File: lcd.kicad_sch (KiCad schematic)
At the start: 9 parts, among them J2 FPC-05F-12PH20, Q1 SS8050

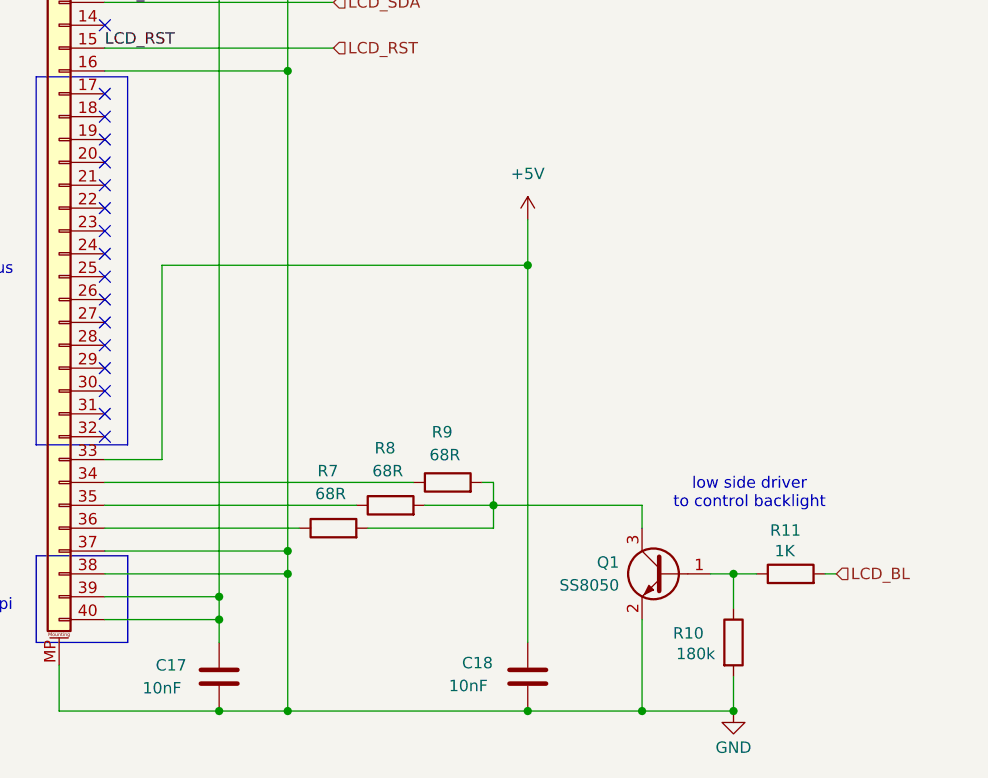
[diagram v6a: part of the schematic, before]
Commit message: small updates in component selection
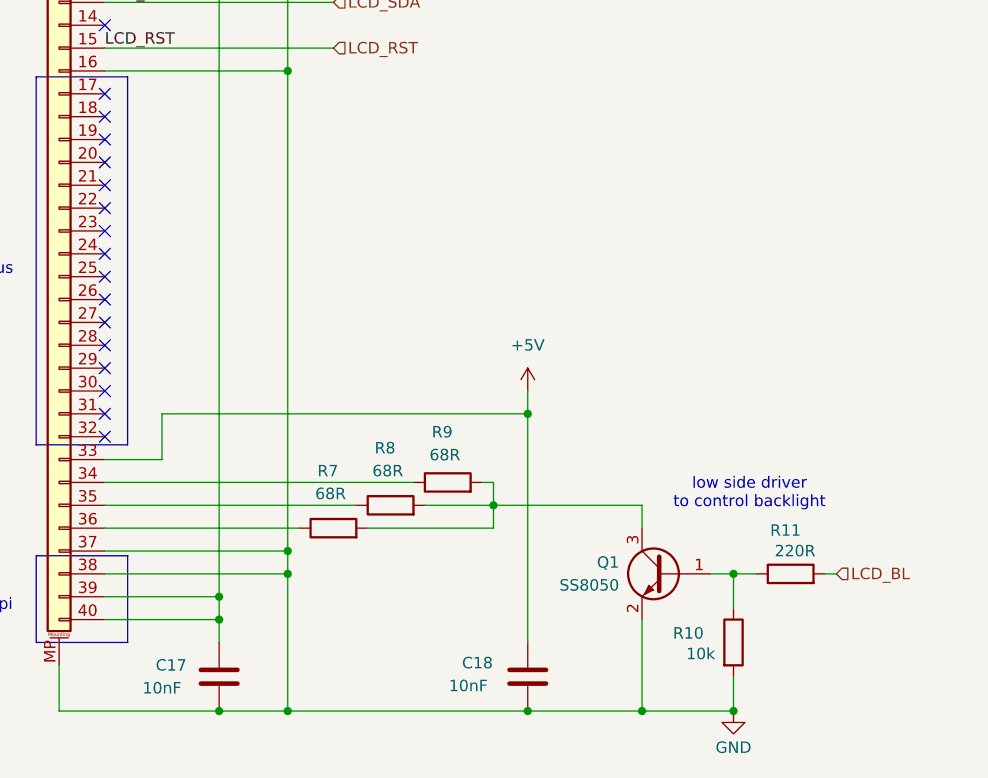
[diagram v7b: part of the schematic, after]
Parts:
- R10: value 180k -> 10k
- R11: value 1K -> 220R
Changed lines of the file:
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@@
-	)
-	(junction
-		(at 121.92 119.38)
-		(diameter 0)
-		(color 0 0 0 0)
 	)
 	(junction
@@
 	)
 	(junction
+		(at 121.92 135.89)
+		(diameter 0)
+		(color 0 0 0 0)
+	)
+	(junction
 		(at 87.63 168.91)
 		(diameter 0)
@@
 	(wire
 		(pts
-			(xy 81.28 140.97) (xy 81.28 119.38)
+			(xy 81.28 140.97) (xy 81.28 135.89)
 		)
 		(stroke
@@
 	(wire
 		(pts
+			(xy 121.92 133.35) (xy 121.92 135.89)
+		)
+		(stroke
+			(width 0)
+			(type default)
+		)
+	)
+	(wire
+		(pts
 			(xy 144.78 157.48) (xy 144.78 153.67)
 		)
@@
 	(wire
 		(pts
-			(xy 81.28 119.38) (xy 121.92 119.38)
+			(xy 81.28 135.89) (xy 121.92 135.89)
 		)
 		(stroke
@@
 	(wire
 		(pts
-			(xy 121.92 114.3) (xy 121.92 119.38)
-		)
-		(stroke
-			(width 0)
-			(type default)
-		)
-	)
-	(wire
-		(pts
 			(xy 74.93 156.21) (xy 87.63 156.21)
 		)
@@
 	(wire
 		(pts
-			(xy 121.92 119.38) (xy 121.92 161.29)
-		)
-		(stroke
-			(width 0)
-			(type default)
-		)
-	)
-	(wire
-		(pts
 			(xy 74.93 153.67) (xy 95.25 153.67)
 		)
@@
 		(pts
 			(xy 134.62 168.91) (xy 144.78 168.91)
+		)
+		(stroke
+			(width 0)
+			(type default)
+		)
+	)
+	(wire
+		(pts
+			(xy 121.92 135.89) (xy 121.92 161.29)
 		)
 		(stroke
@@
 	(symbol
 		(lib_id "power:+5V")
-		(at 121.92 114.3 0)
+		(at 121.92 133.35 0)
 		(unit 1)
 		(exclude_from_sim no)
@@
 		(fields_autoplaced yes)
 		(property "Reference" "#PWR033"
-			(at 121.92 118.11 0)
+			(at 121.92 137.16 0)
 			(effects
 				(font
@@
 		)
 		(property "Value" "+5V"
-			(at 121.92 109.22 0)
+			(at 121.92 128.27 0)
 			(effects
 				(font
@@
 		)
 		(property "Footprint" ""
-			(at 121.92 114.3 0)
+			(at 121.92 133.35 0)
 			(effects
 				(font
@@
 		)
 		(property "Datasheet" ""
-			(at 121.92 114.3 0)
+			(at 121.92 133.35 0)
 			(effects
 				(font
@@
 		)
 		(property "Description" "Power symbol creates a global label with name \"+5V\""
-			(at 121.92 114.3 0)
+			(at 121.92 133.35 0)
 			(effects
 				(font
@@
 			)
 		)
-		(property "Value" "180k"
+		(property "Value" "10k"
 			(at 142.748 162.56 0)
 			(effects
@@
 			)
 		)
-		(property "Value" "1K"
+		(property "Value" "220R"
 			(at 149.352 151.13 90)
 			(effects

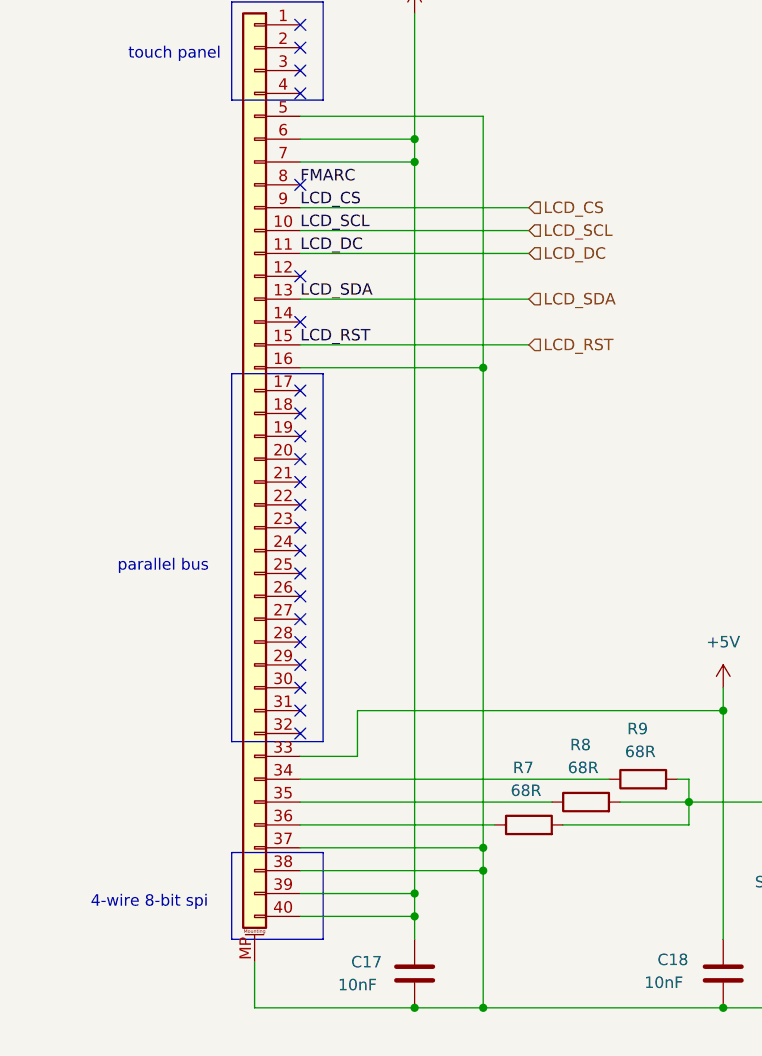
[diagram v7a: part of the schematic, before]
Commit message: check with hardware manual, add comments, add mpns
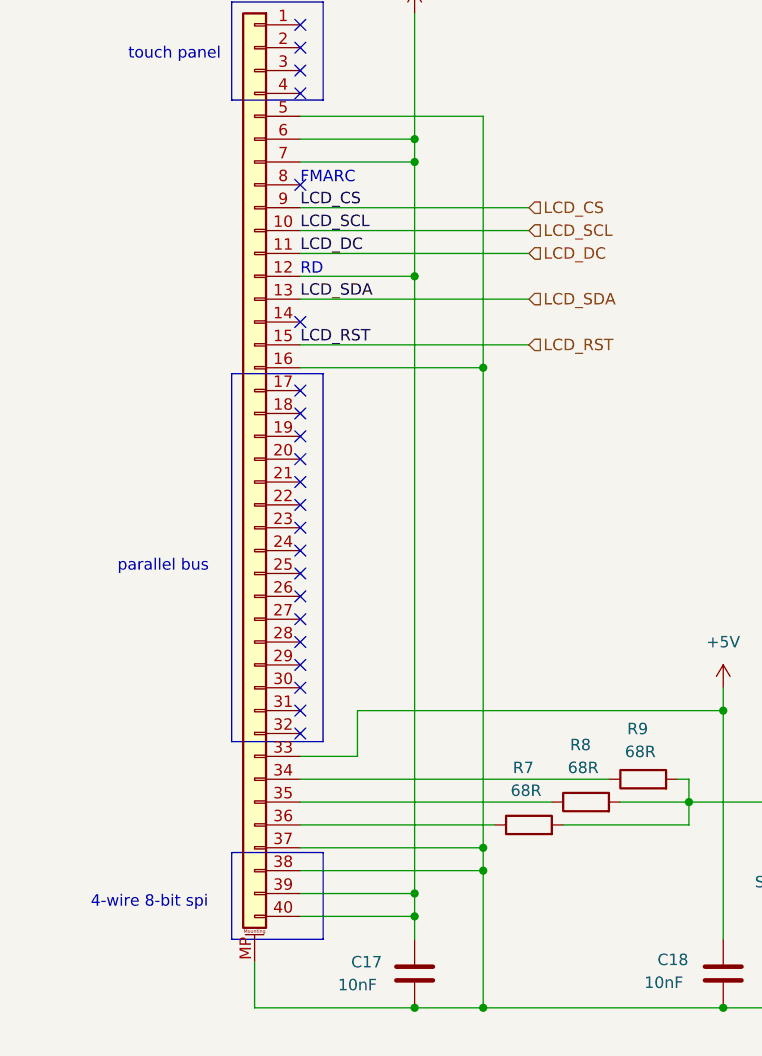
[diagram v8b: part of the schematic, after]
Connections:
- net +3V3: now also J2.12 (Pin_12)
- net FMARC: no longer names the net of J2.8 (Pin_8)
- no-connect marks 23 -> 22
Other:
- note added: "FMARC"
- note added: "RD"
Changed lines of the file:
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@@
+		)
+	)
+	(text "RD"
+		(exclude_from_sim no)
+		(at 74.93 87.63 0)
+		(effects
+			(font
+				(size 1.27 1.27)
+			)
+			(justify left bottom)
+		)
+	)
+	(text "FMARC"
+		(exclude_from_sim no)
+		(at 74.93 77.47 0)
+		(effects
+			(font
+				(size 1.27 1.27)
+			)
+			(justify left bottom)
 		)
 	)
@@
 	)
 	(junction
+		(at 87.63 87.63)
+		(diameter 0)
+		(color 0 0 0 0)
+	)
+	(junction
 		(at 95.25 97.79)
 		(diameter 0)
@@
 	)
 	(no_connect
-		(at 74.93 87.63)
-	)
-	(no_connect
 		(at 74.93 77.47)
 	)
@@
 	(wire
 		(pts
-			(xy 87.63 74.93) (xy 87.63 156.21)
+			(xy 87.63 74.93) (xy 87.63 87.63)
 		)
 		(stroke
@@
 	(wire
 		(pts
+			(xy 87.63 87.63) (xy 87.63 156.21)
+		)
+		(stroke
+			(width 0)
+			(type default)
+		)
+	)
+	(wire
+		(pts
 			(xy 87.63 156.21) (xy 87.63 158.75)
 		)
@@
 		(pts
 			(xy 134.62 158.75) (xy 134.62 168.91)
+		)
+		(stroke
+			(width 0)
+			(type default)
+		)
+	)
+	(wire
+		(pts
+			(xy 74.93 87.63) (xy 87.63 87.63)
 		)
 		(stroke
@@
 		(effects
 			(font
-				(size 1.27 1.27)
-			)
-			(justify left bottom)
-		)
-	)
-	(label "FMARC"
-		(at 74.93 77.47 0)
-		(effects
-			(font
